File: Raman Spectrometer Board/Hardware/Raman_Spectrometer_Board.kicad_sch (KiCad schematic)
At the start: 5 parts, among them J1 RJ45_LED_Shielded, U1 Teensy4.1_DEV-16771

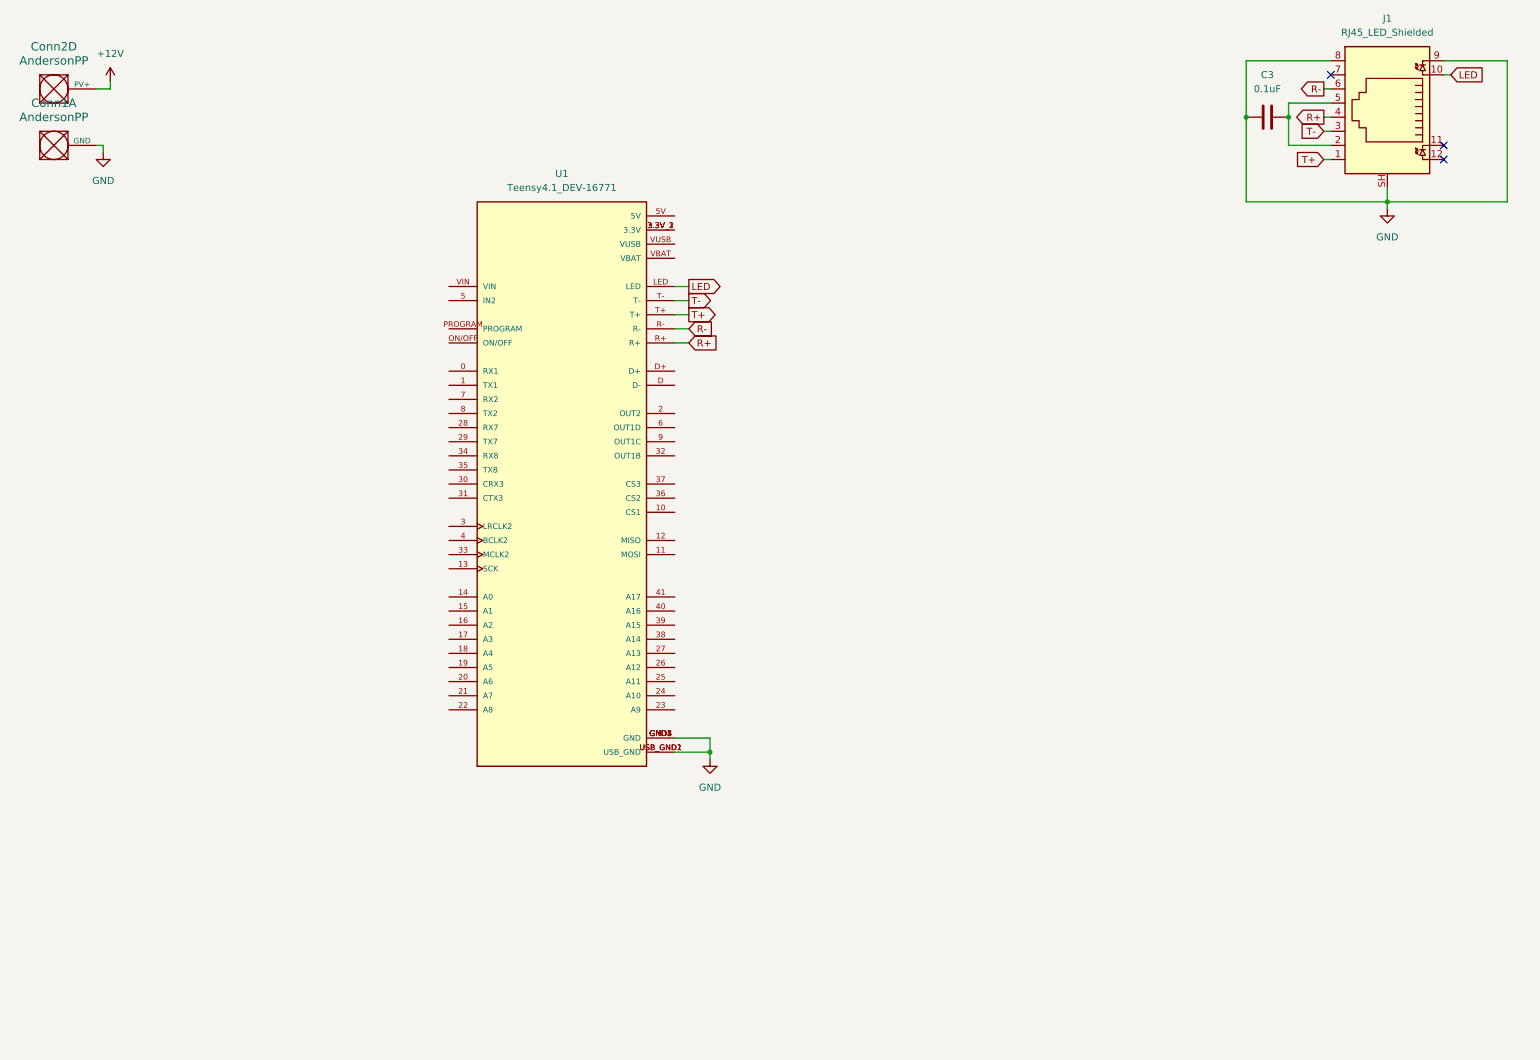
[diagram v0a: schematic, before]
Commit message: Finshed CCD breakout
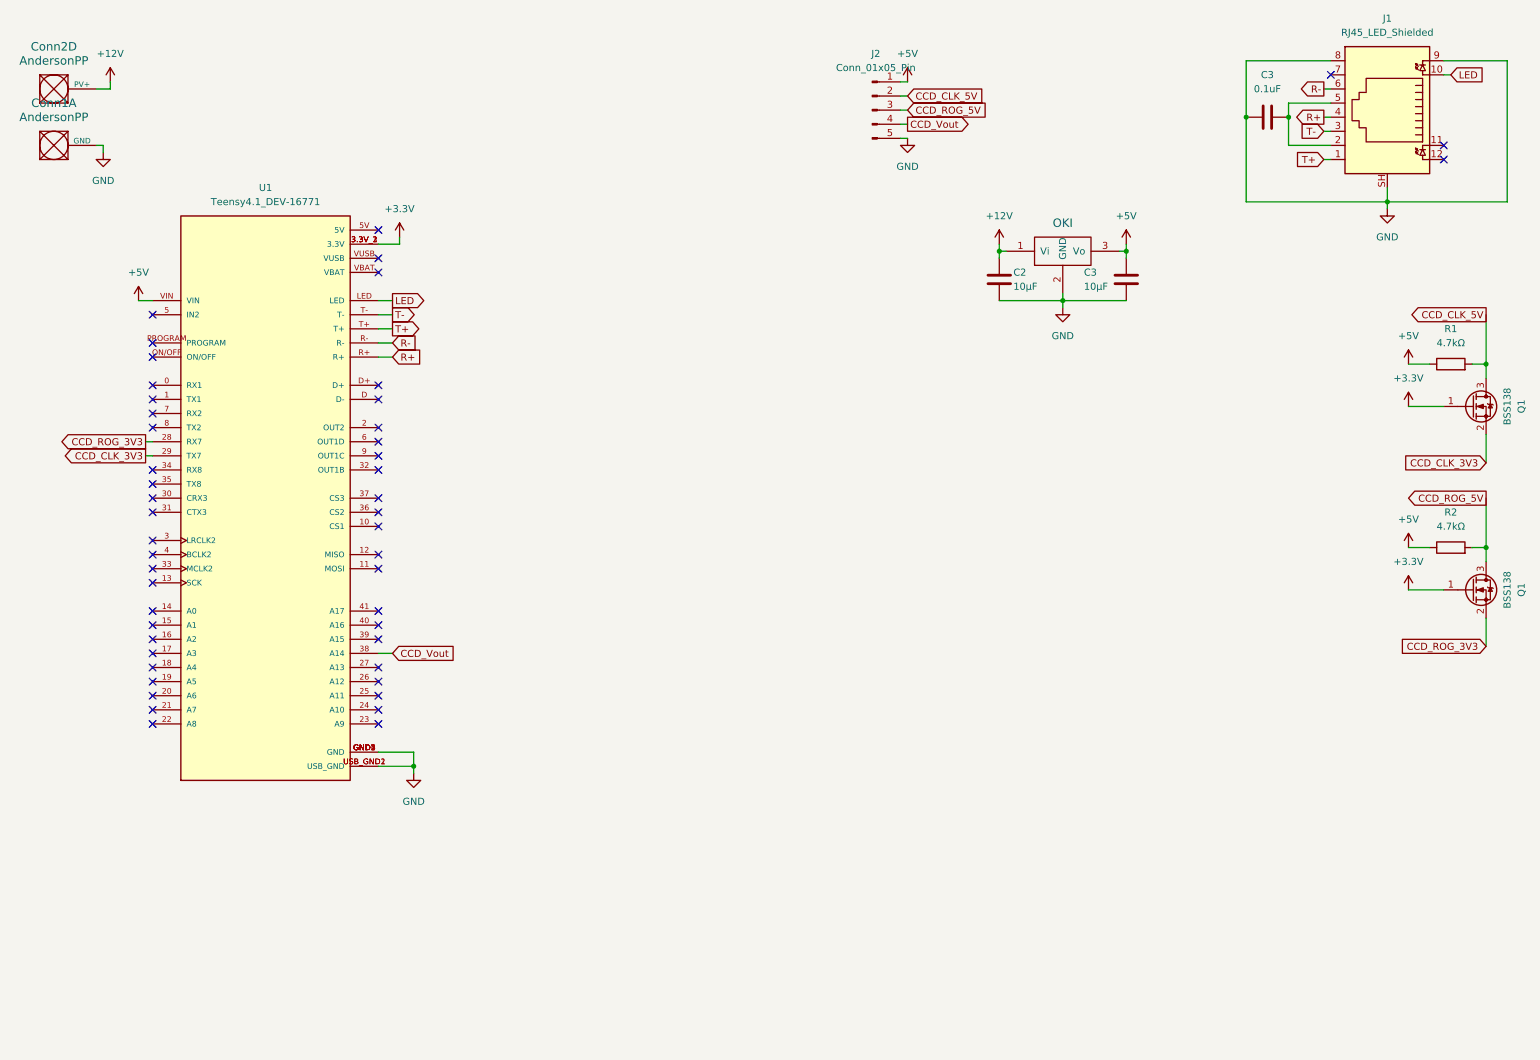
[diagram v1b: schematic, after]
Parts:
- added C2, C3: 10µF, symbol Device:C
- added J2: Conn_01x05_Pin, symbol Connector:Conn_01x05_Pin
- added Q1 (x2): BSS138, Package_TO_SOT_SMD:SOT-23, symbol Transistor_FET:BSS138
- added R1, R2: 4.7kΩ, symbol Device:R
- added U2: OKI, symbol MRDT_Devices:OKI
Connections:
- net +12V: now also C2.1, U2.1 (Vi)
- net GND: now also C2.2, C3.2, J2.5 (Pin_5), U2.2 (GND)
- net CCD_ROG_3V3: now reaches U1.28 (RX7)
- net CCD_ROG_3V3: now also Q1.2 (S)
- net CCD_CLK_3V3: now reaches U1.29 (TX7)
- net CCD_CLK_3V3: now also Q1.2 (S)
- net +3.3V: now reaches U1.3.3V_1 (3.3V), U1.3.3V_2 (3.3V), U1.3.3V_3 (3.3V)
- net +3.3V: now also Q1.1 (G), Q1.1 (G)
- net CCD_Vout: now reaches U1.38 (A14)
- net CCD_Vout: now also J2.4 (Pin_4)
- net +5V: now reaches U1.VIN
- net +5V: now also C3.1, J2.1 (Pin_1), R1.1, R2.1, U2.3 (Vo)
- new net CCD_CLK_5V: J2.2 (Pin_2), Q1.3 (D), R1.2
- new net CCD_ROG_5V: J2.3 (Pin_3), Q1.3 (D), R2.2
- no-connect marks 3 -> 49
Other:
- moved on the sheet: U1

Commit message: added laser breakout to raman board
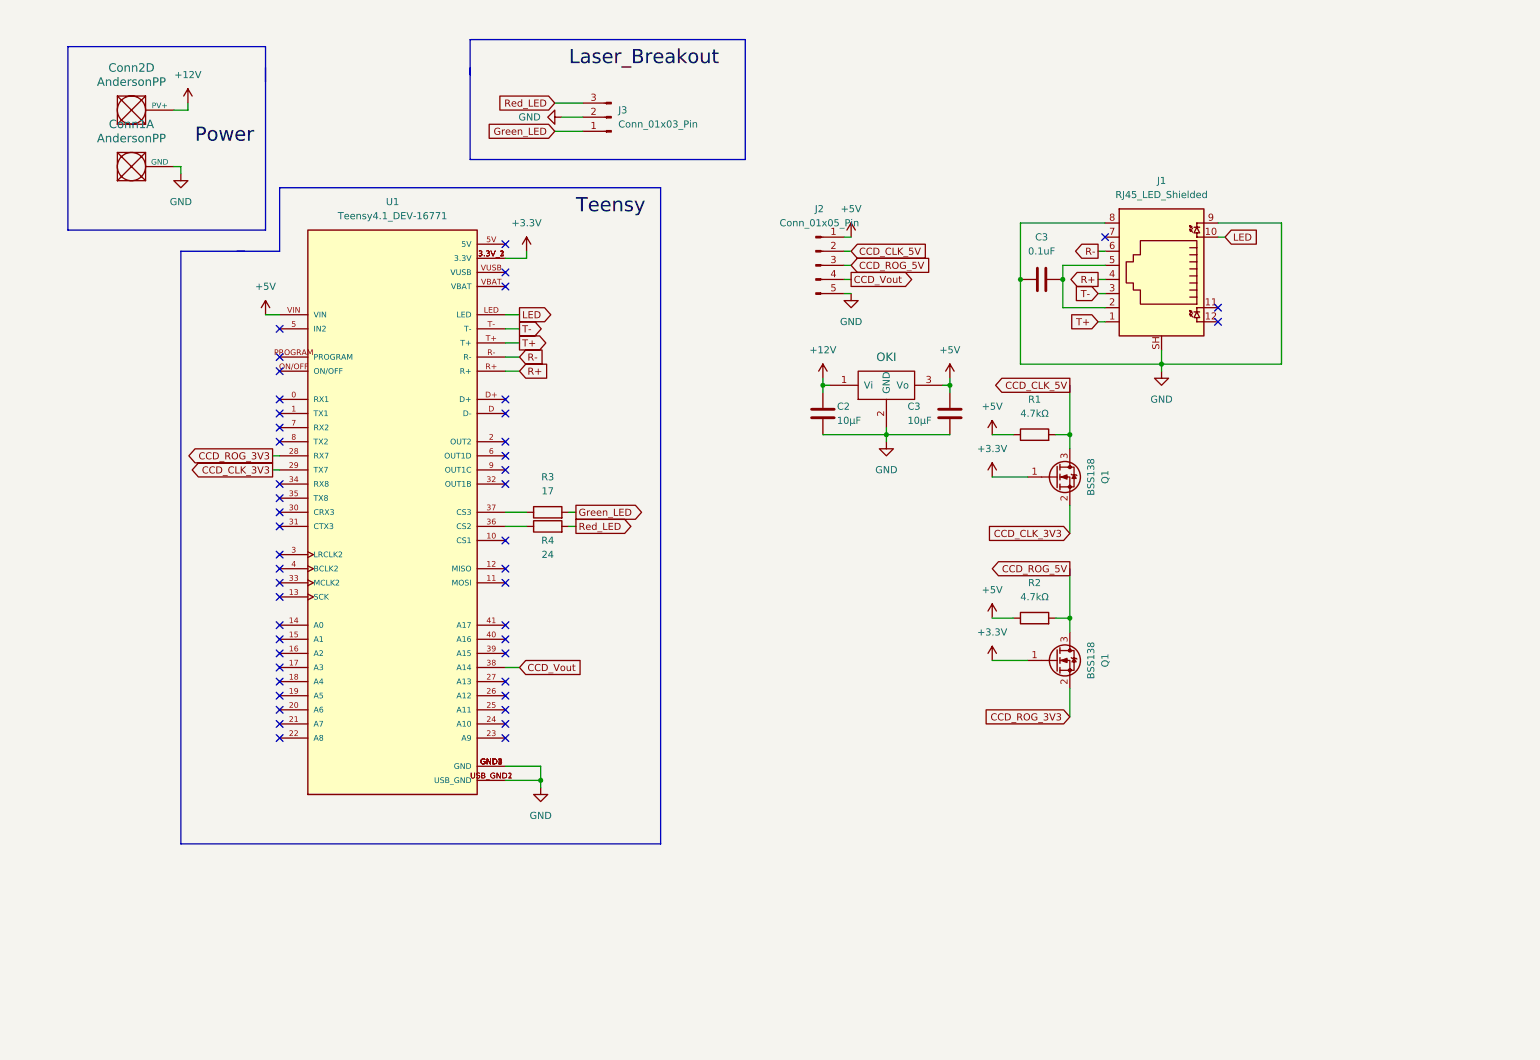
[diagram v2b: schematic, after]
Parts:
- added J3: Conn_01x03_Pin, symbol Connector:Conn_01x03_Pin
- added R3: 17, symbol Device:R
- added R4: 24, symbol Device:R
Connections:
- net GND: now also J3.2 (Pin_2)
- net at U1.36 (CS2): now also R4.1
- net at U1.37 (CS3): now also R3.1
- new net Green_LED: J3.1 (Pin_1), R3.2
- new net Red_LED: J3.3 (Pin_3), R4.2
- no-connect marks 49 -> 47
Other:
- moved on the sheet: C2, C3, Conn1A, Conn2D, J1, J2, Q1, R1, R2, U1

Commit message: finished adding boxes to ramen board
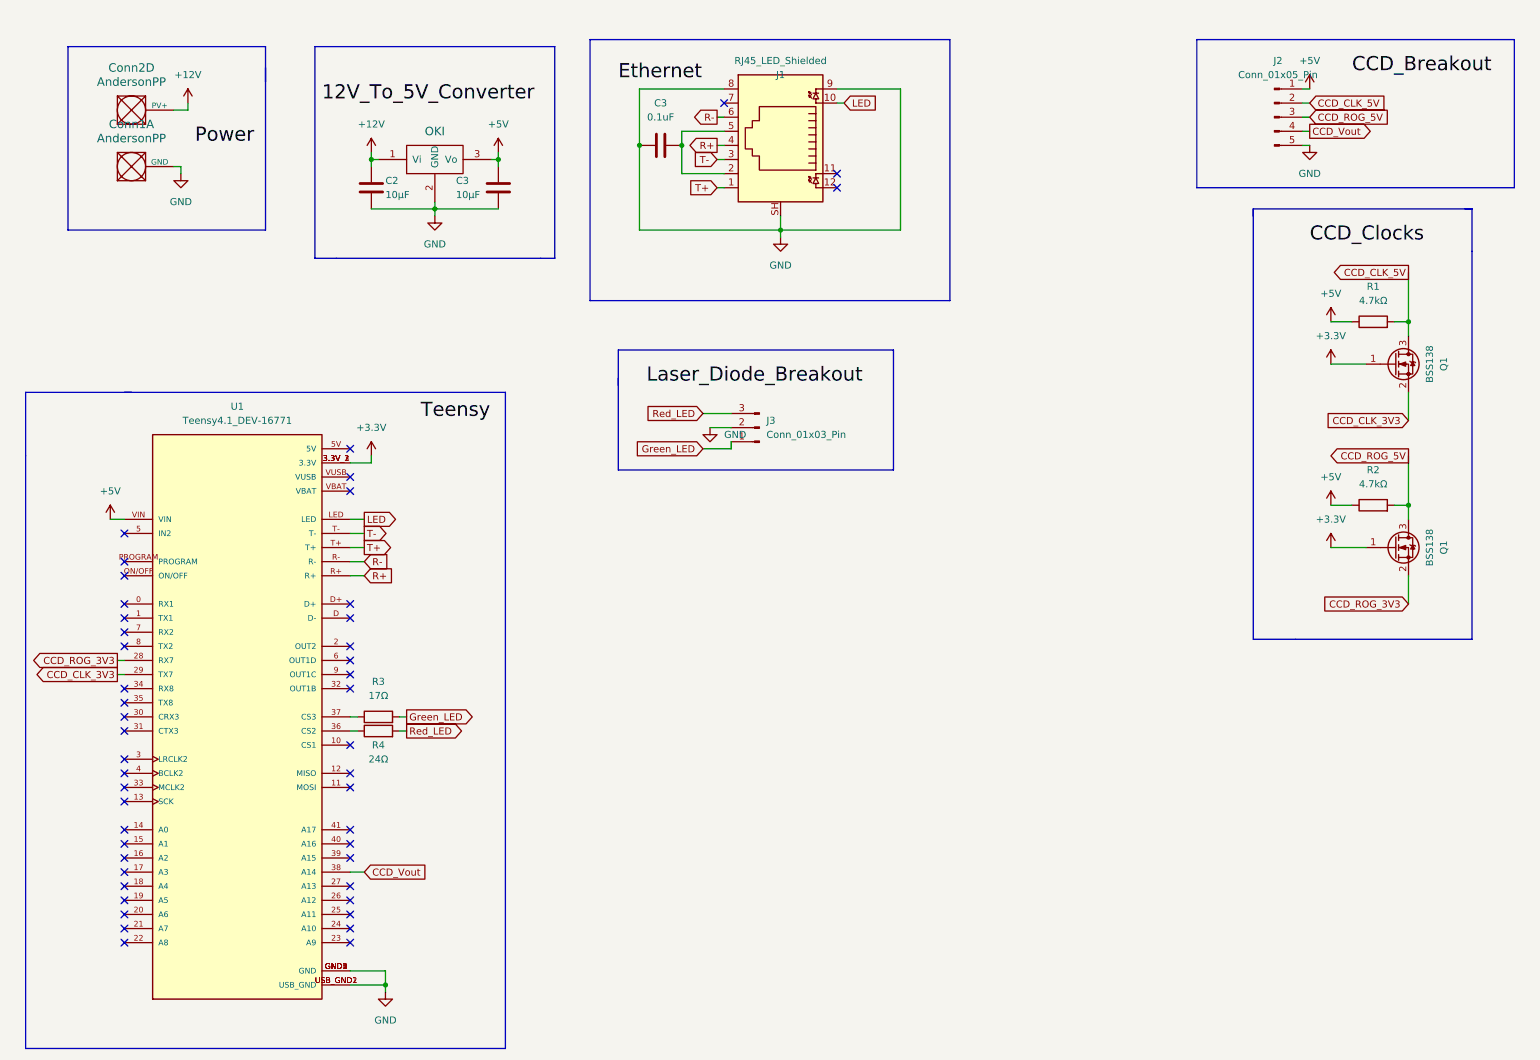
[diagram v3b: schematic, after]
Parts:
- R3: value 17 -> 17Ω
- R4: value 24 -> 24Ω
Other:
- moved on the sheet: C2, C3, J1, J2, J3, Q1, R1, R2, R3, R4, U1

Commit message: I forgot to save everything for the last commit
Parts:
- U2: footprint (none) -> MRDT_Devices:OKI_Horizontal
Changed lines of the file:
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@@
       (effects (font (size 1.524 1.524)))
     )
-    (property "Footprint" "" (at 77.47 40.64 0)
+    (property "Footprint" "MRDT_Devices:OKI_Horizontal" (at 77.47 40.64 0)
       (effects (font (size 1.524 1.524)) hide)
     )
